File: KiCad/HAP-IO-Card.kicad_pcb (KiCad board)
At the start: 2 copper layers, 110 x 72 mm, 201 parts, among them CON601 AVR-JTAG-10, J201 DI1, J202 DI2, J203 DI3, J204 DI4, J205 DI5, J206 DI6, J207 DI7, J208 DI8, J209 DO1/2, J210 DO3/4, J211 DO5/6, J212 DO7/8, J213 GND, J214 GND, J215 GND, J216 GND, J401 AI1, J402 AI2, J403 AI3, J404 AI4, J405 AI5, J406 AI6, J407 AI7, J408 AI8, J501 12V, J601 ISP0, J602 ISP1, J603 CONN_01X02, J604 CONN_01X02, J605 CONN_01X02, J606 CONN_01X02, J607 CONN_01X03, J608 CONN_01X03, J701 NEO1, J702 5V_I/O_2, J703 5V_I/O_1, J704 NEO1, J705 NEO1, J706 NEO1, J707 NeoPixel, Q201 ZXTN25050DFHTA, Q202 ZXTN25050DFHTA, Q203 ZXTN25050DFHTA, Q204 ZXTN25050DFHTA, Q205 ZXTN25050DFHTA, Q206 ZXTN25050DFHTA, Q207 ZXTN25050DFHTA, Q208 ZXTN25050DFHTA, U201 LTV-354T, U202 LTV-354T, U203 LTV-354T, U204 LTV-354T, U205 LTV-354T, U206 LTV-354T, U207 LTV-354T, U208 LTV-354T, U209 MCP23017, U401 ADS1115IDGST, U402 ADS1115IDGST, U501 LM1086-5V, U502 LM1086-3.3V, U701 TXB0102DCT

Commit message: Remade layout
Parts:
- C201, C202, C203, C204, C205, C206, C207, C208, C409, C410, C701, C702, C704, R209, R210, R211, R212, R213, R214, R215, R216, R237, R238, R249, R250, R409, R410, R411, R412, U401, U402, U701: moved to F.Cu
- D215, D216, D217, D218, D219, D220, D223, D224: footprint Diodes_THT:D_DO-41_SOD81_P5.08mm_Vertical_KathodeUp -> Diodes_THT:D_DO-41_SOD81_P2.54mm_Vertical_KathodeUp
- J701: value NEO1 -> 5V_I/O_2; footprint Pin_Headers:Pin_Header_Straight_1x04_Pitch1.27mm -> Pin_Headers:Pin_Header_Straight_1x02_Pitch2.54mm
- J702: value 5V_I/O_2 -> 5V_I/O_1
- J703: value 5V_I/O_1 -> NEO1; footprint Pin_Headers:Pin_Header_Straight_1x02_Pitch2.54mm -> Pin_Headers:Pin_Header_Straight_1x04_Pitch1.27mm
- J704: value NEO1 -> NEO2
- J705: value NEO1 -> NEO3
- J706: value NEO1 -> NEO4
- J707: value NeoPixel -> CONN_01X03; footprint Pin_Headers:Pin_Header_Straight_1x01_Pitch2.54mm -> Pin_Headers:Pin_Header_Straight_1x03_Pitch2.54mm
- R225, R226, R227, R228, R229, R230: value 180 -> 10k; moved to F.Cu
- R231, R232: value 470 -> 10k; moved to F.Cu
- R233, R234, R235, R236: value 470 -> 180; moved to F.Cu
- R241, R242, R243, R244, R247, R248: value 10k -> 470
- R245, R246: value 10k -> 180; moved to F.Cu
- moved J603 142.0 mm to (-35.8, 19.5)
- moved J604 142.0 mm to (-26.3, 19.5)
- moved J605 142.0 mm to (-18.3, 19.5)
- moved J606 142.0 mm to (-10.3, 19.5)
- moved J607 142.0 mm to (-12.8, 24.0)
- moved J608 142.0 mm to (-12.8, 28.0)
- moved J707 102.7 mm to (193.7, -11.5)
- moved J701 101.1 mm to (179.2, -13.5)
- moved J703 101.1 mm to (179.7, -17.5)
- moved J704 101.1 mm to (186.7, -13.5)
- moved J705 101.1 mm to (179.2, -9.03)
- moved J706 101.1 mm to (186.7, -9.03)
- moved R225 83.5 mm to (50.2, 36.5), turned to 270 degrees
- moved J702 82.1 mm to (192.2, -20.5)
- moved R250 78.4 mm to (154.7, -16.0), turned to 270 degrees
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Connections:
- J701 pad 1: Net-(C704-Pad1) -> GND
- J701 pad 2: POWER5V -> Net-(C703-Pad1)
- J702 pad 1: Net-(C703-Pad1) -> GND
- J702 pad 2: GND -> Net-(C704-Pad1)
- J703 pad 2: GND -> POWER5V
- J704 pad 1: Net-(J701-Pad4) -> Net-(J703-Pad4)
- J707 pad 1: Net-(J706-Pad4) -> GND
- R225 pad 2: Net-(D209-Pad2) -> DI1
- R226 pad 2: Net-(D210-Pad2) -> DI2
- R227 pad 2: Net-(D211-Pad2) -> DI3
- R228 pad 2: Net-(D212-Pad2) -> DI4
- R229 pad 2: Net-(D213-Pad2) -> DI5
- R230 pad 2: Net-(D214-Pad2) -> DI6
- R231 pad 1: Net-(Q201-Pad1) -> POWER3V3
- R231 pad 2: DO1 -> DI7
- R232 pad 1: Net-(Q202-Pad1) -> POWER3V3
- R232 pad 2: DO2 -> DI8
- R233 pad 1: Net-(Q203-Pad1) -> POWER3V3
- R233 pad 2: DO3 -> Net-(D209-Pad2)
- R234 pad 1: Net-(Q204-Pad1) -> POWER3V3
- R234 pad 2: DO4 -> Net-(D210-Pad2)
- R235 pad 1: Net-(Q205-Pad1) -> POWER3V3
- R235 pad 2: DO5 -> Net-(D211-Pad2)
- R236 pad 1: Net-(Q206-Pad1) -> POWER3V3
- R236 pad 2: DO6 -> Net-(D212-Pad2)
- R237 pad 2: Net-(D221-Pad2) -> Net-(D213-Pad2)
- R238 pad 2: Net-(D222-Pad2) -> Net-(D214-Pad2)
- R239 pad 1: Net-(Q207-Pad1) -> Net-(Q201-Pad1)
- R239 pad 2: DO7 -> DO1
- R240 pad 1: Net-(Q208-Pad1) -> Net-(Q202-Pad1)
- R240 pad 2: DO8 -> DO2
- R241 pad 1: POWER3V3 -> Net-(Q203-Pad1)
- R241 pad 2: DIGITAL_INTB -> DO3
- R242 pad 1: POWER3V3 -> Net-(Q204-Pad1)
- R242 pad 2: DIGITAL_INTA -> DO4
- R243 pad 1: POWER3V3 -> Net-(Q205-Pad1)
- R243 pad 2: DI1 -> DO5
- R244 pad 1: POWER3V3 -> Net-(Q206-Pad1)
- R244 pad 2: DI2 -> DO6
- R245 pad 2: DI3 -> Net-(D221-Pad2)
- R246 pad 2: DI4 -> Net-(D222-Pad2)
- R247 pad 1: POWER3V3 -> Net-(Q207-Pad1)
- R247 pad 2: DI5 -> DO7
- R248 pad 1: POWER3V3 -> Net-(Q208-Pad1)
- R248 pad 2: DI6 -> DO8
- R249 pad 2: DI7 -> DIGITAL_INTB
- R250 pad 2: DI8 -> DIGITAL_INTA
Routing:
- net POWER3V3: track 77.8 -> 0.00 mm, vias 4 -> 0
- net ANALOG_RDY_1: track 57.1 -> 0.00 mm
- net DI8: track 54.5 -> 0.00 mm
- net DI7: track 50.0 -> 0.00 mm
- net DI6: track 44.6 -> 0.00 mm
- net ANALOG_SDA: track 41.4 -> 0.00 mm, vias 3 -> 0
- net DI5: track 40.1 -> 0.00 mm
- net ANALOG_SCL: track 38.2 -> 0.00 mm, vias 2 -> 0
- net DI4: track 28.9 -> 0.00 mm, vias 2 -> 0
- net ANALOG_RDY_2: track 27.1 -> 0.00 mm, vias 2 -> 0
- net DI1: track 24.1 -> 0.00 mm
- net DI3: track 23.4 -> 0.00 mm
- net AI4: track 22.5 -> 0.00 mm
- net AI5: track 22.4 -> 0.00 mm
- net AI1: track 22.1 -> 0.00 mm
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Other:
- board text added: "LogDbg"

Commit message: Before starting traces
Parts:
- C703: moved to F.Cu
- moved C703 140.6 mm to (51.2, 55.3), turned to 90 degrees
- moved C704 132.8 mm to (48.2, 55.3)
- moved C702 130.5 mm to (60.2, 55.3)
- moved U701 130.5 mm to (55.7, 55.3), turned to 0 degrees
- moved C701 129.3 mm to (59.2, 58.3), turned to 0 degrees
- moved C209 128.0 mm to (67.2, 55.5)
- moved R701 121.7 mm to (57.2, 51.3), turned to 0 degrees
- moved U209 111.0 mm to (78.0, 55.7), turned to 270 degrees
- moved J603 106.7 mm to (49.2, 83.9), turned to 0 degrees
- moved J604 102.7 mm to (53.7, 83.9), turned to 0 degrees
- moved J608 101.3 mm to (73.2, 81.4), turned to 0 degrees
- moved J605 100.0 mm to (58.2, 83.9), turned to 0 degrees
- moved J607 99.3 mm to (68.2, 81.4), turned to 0 degrees
- moved J606 97.8 mm to (63.2, 83.9), turned to 0 degrees
- moved R250 97.5 mm to (91.2, 58.0), turned to 0 degrees
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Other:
- board text added: "EspPwr"

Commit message: Save...
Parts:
- moved R232 2.90 mm to (124.6, 37.0)
- moved R223 2.57 mm to (110.2, 37.0), turned to 90 degrees
- moved R222 2.55 mm to (99.2, 37.0), turned to 90 degrees
- moved R230 2.55 mm to (101.7, 37.0)
- moved R231 2.52 mm to (112.7, 37.0)
- moved R224 2.20 mm to (122.1, 37.0), turned to 90 degrees
- moved C704 1.01 mm to (47.2, 55.5)
- moved R209 0.71 mm to (45.2, 33.0)
- moved R210 0.71 mm to (54.7, 33.0)
- moved R211 0.71 mm to (64.2, 33.0)
- moved C701 0.66 mm to (59.2, 59.0)
- moved C702 0.53 mm to (60.7, 55.5)
- moved C703 0.53 mm to (50.7, 55.5)
- moved C201 0.50 mm to (48.7, 40.0)
- moved C202 0.50 mm to (58.2, 40.0)
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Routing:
- net Net-(J202-Pad2): track 0.00 -> 6.23 mm
- net Net-(R201-Pad1): track 0.00 -> 5.61 mm, vias 0 -> 1
- net Net-(R202-Pad1): track 0.00 -> 5.41 mm, vias 0 -> 1
- net Net-(J202-Pad1): track 0.00 -> 5.34 mm
- net Net-(J201-Pad2): track 0.00 -> 5.00 mm
- net Net-(J201-Pad1): track 0.00 -> 4.41 mm
- net Net-(C202-Pad1): track 0.00 -> 3.41 mm
- net Net-(C201-Pad1): track 0.00 -> 3.41 mm
- net DI1: track 0.00 -> 2.80 mm
- net DI2: track 0.00 -> 2.80 mm
- net Net-(D201-Pad2): track 0.00 -> 1.03 mm
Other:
- board text added: "HAP I/O Card (C) Per Malmberg"

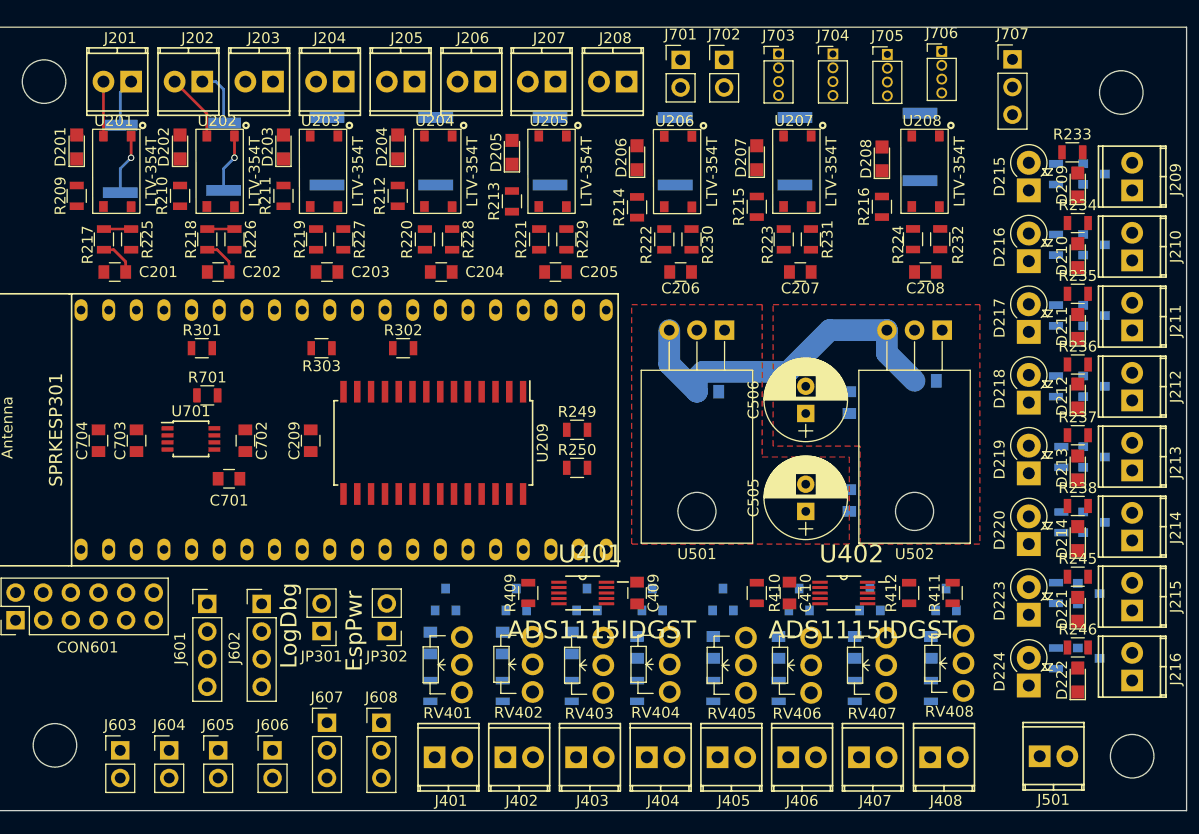
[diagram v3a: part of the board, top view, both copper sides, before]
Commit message: Before reworking analog inputs.
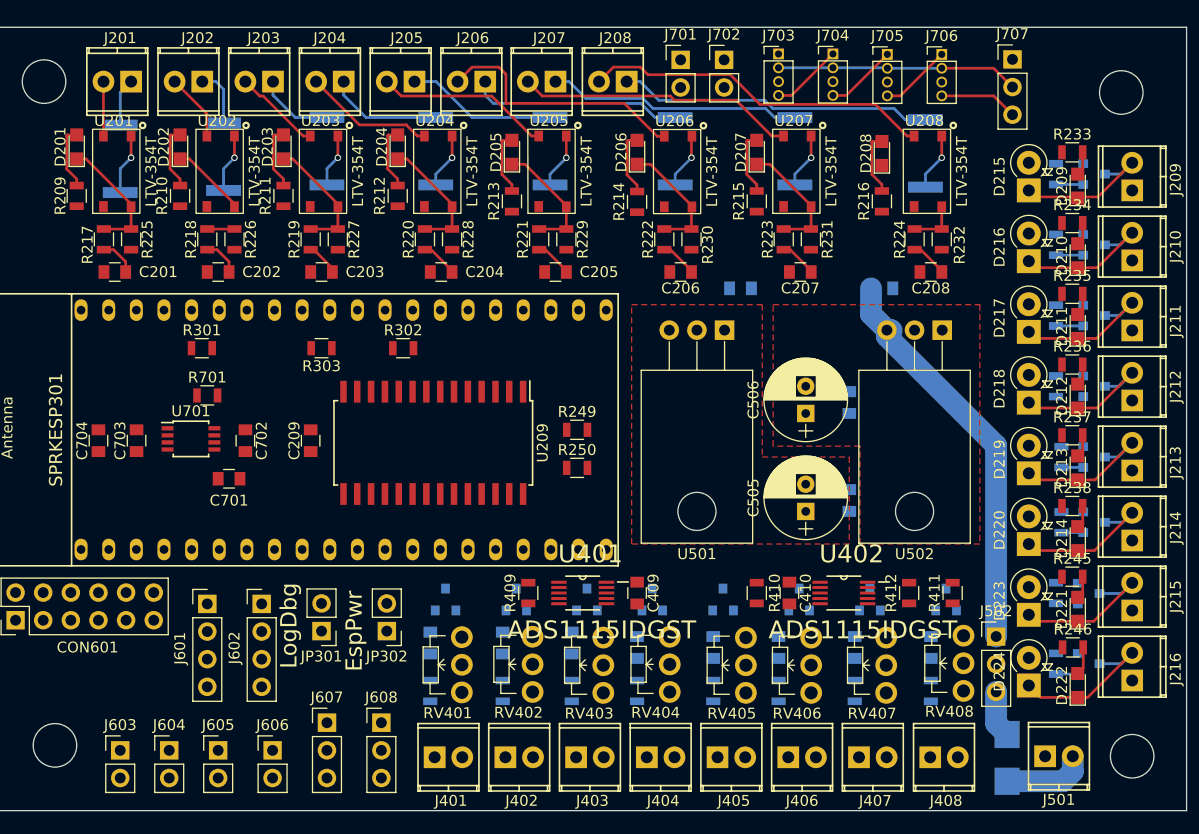
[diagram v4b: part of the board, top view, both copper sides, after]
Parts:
- added D501: MBR340, Diodes_SMD:D_SMB, B.Cu at (130.7, 84.6)
- added J502: CONN_01X03_FEMALE, Pin_Headers:Pin_Header_Straight_1x03_Pitch2.54mm, F.Cu at (129.7, 73.5)
- moved C501 9.96 mm to (106.2, 41.5)
- moved C502 9.39 mm to (119.2, 41.5)
- moved R208 0.78 mm to (123.2, 29.1)
- moved C203 0.50 mm to (67.7, 40.0)
- moved C208 0.50 mm to (123.7, 40.0)
- moved D206 0.50 mm to (96.7, 29.0)
- moved D207 0.50 mm to (107.7, 29.0)
- moved D208 0.50 mm to (119.2, 29.1)
- moved D222 0.50 mm to (137.2, 78.0)
- moved J501 0.50 mm to (134.2, 84.5)
- moved Q208 0.50 mm to (138.2, 76.0)
- moved R214 0.50 mm to (96.7, 33.5)
- moved R215 0.50 mm to (107.7, 33.5)
- moved R216 0.50 mm to (119.2, 33.5)
- moved R219 0.50 mm to (66.7, 37.0)
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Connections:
- J501 pad 2: /Powersupply/Input12V -> /Powersupply/Input12VOutside
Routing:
- net Net-(J208-Pad2): track 0.00 -> 32.1 mm
- net Net-(J208-Pad1): track 0.00 -> 28.9 mm
- net Net-(J207-Pad2): track 0.00 -> 25.6 mm
- net Net-(J206-Pad2): track 0.00 -> 23.7 mm
- net Net-(J207-Pad1): track 0.00 -> 23.4 mm
- net POWER5V: track 0.00 -> 22.2 mm
- net Net-(J206-Pad1): track 0.00 -> 19.6 mm
- net Net-(J205-Pad2): track 0.00 -> 16.0 mm
- net Net-(D222-Pad1): track 0.00 -> 15.1 mm
- net Net-(D221-Pad1): track 0.00 -> 14.6 mm
- net Net-(D213-Pad1): track 0.00 -> 14.2 mm
- net Net-(D211-Pad1): track 0.00 -> 14.1 mm
- net Net-(D212-Pad1): track 0.00 -> 14.1 mm
- net Net-(D214-Pad1): track 0.00 -> 14.0 mm
- net Net-(D210-Pad1): track 0.00 -> 14.0 mm
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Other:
- net class Input12VOutside added: clearance 0.2, trace_width 2, via_dia 0.6, via_drill 0.4
- net class Input12VOutside2 added: clearance 0.2, trace_width 2, via_dia 0.6, via_drill 0.4

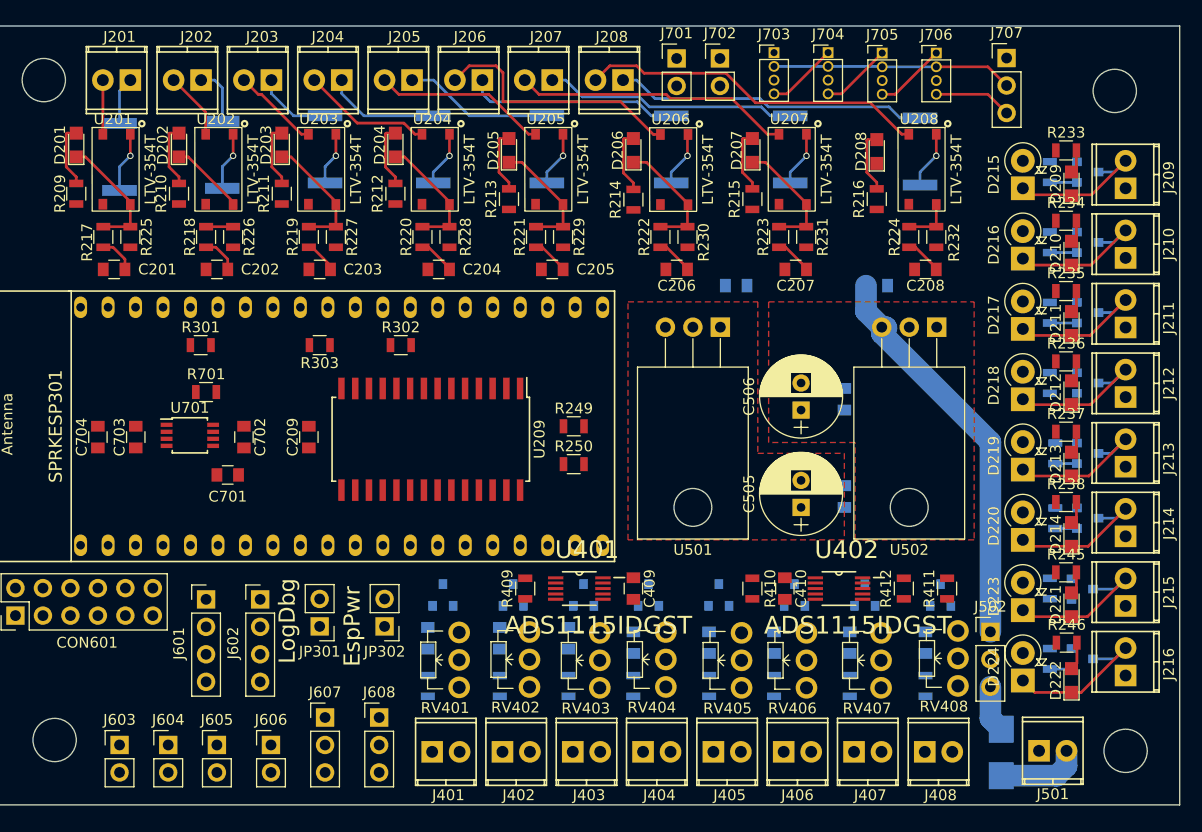
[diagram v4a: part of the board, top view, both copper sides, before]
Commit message: Inputs reworked. New terminals
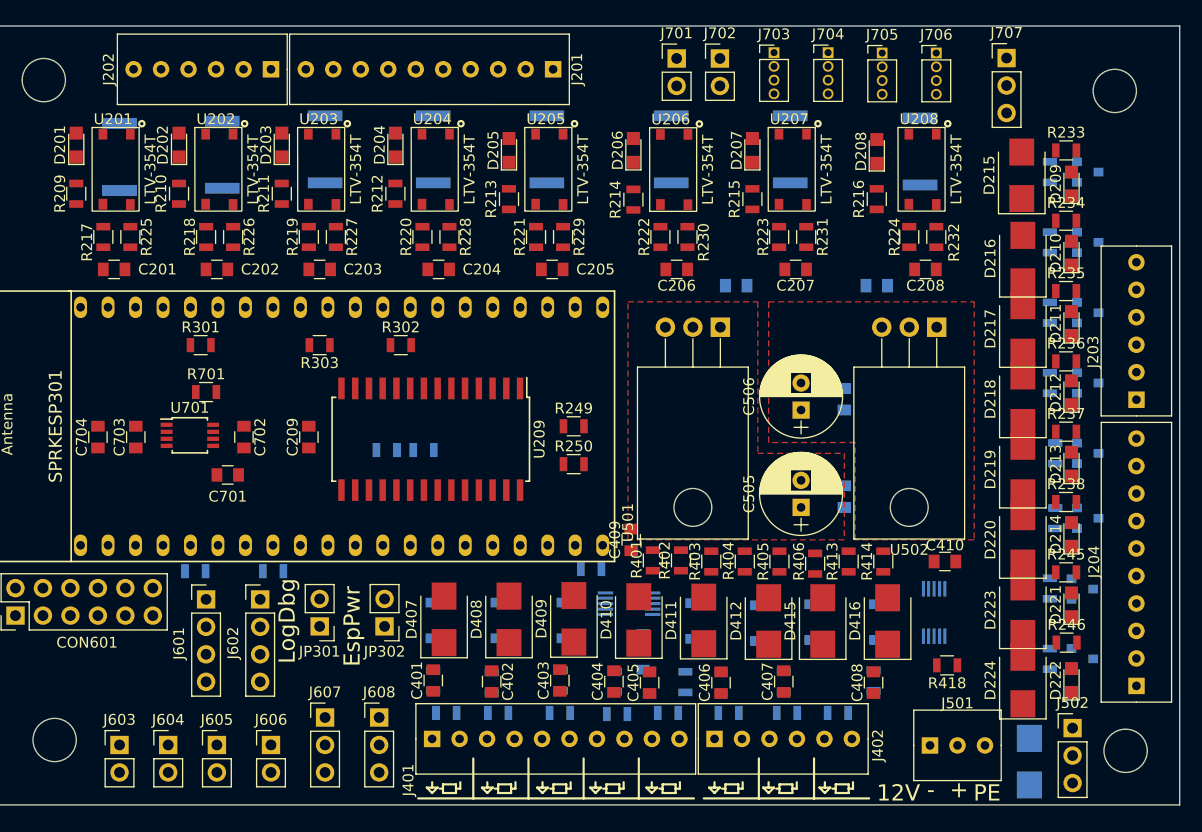
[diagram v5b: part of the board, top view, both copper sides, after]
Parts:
- removed J205: DI5, Connectors_Terminal_Blocks:TerminalBlock_Pheonix_MPT-2.54mm_2pol
- removed J206: DI6, Connectors_Terminal_Blocks:TerminalBlock_Pheonix_MPT-2.54mm_2pol
- removed J207: DI7, Connectors_Terminal_Blocks:TerminalBlock_Pheonix_MPT-2.54mm_2pol
- removed J208: DI8, Connectors_Terminal_Blocks:TerminalBlock_Pheonix_MPT-2.54mm_2pol
- removed J209: DO1/2, Connectors_Terminal_Blocks:TerminalBlock_Pheonix_MPT-2.54mm_2pol
- removed J210: DO3/4, Connectors_Terminal_Blocks:TerminalBlock_Pheonix_MPT-2.54mm_2pol
- removed J211: DO5/6, Connectors_Terminal_Blocks:TerminalBlock_Pheonix_MPT-2.54mm_2pol
- removed J212: DO7/8, Connectors_Terminal_Blocks:TerminalBlock_Pheonix_MPT-2.54mm_2pol
- removed J213, J214, J215, J216: GND, Connectors_Terminal_Blocks:TerminalBlock_Pheonix_MPT-2.54mm_2pol
- removed J403: AI3, Connectors_Terminal_Blocks:TerminalBlock_Pheonix_MPT-2.54mm_2pol
- removed J404: AI4, Connectors_Terminal_Blocks:TerminalBlock_Pheonix_MPT-2.54mm_2pol
- removed J405: AI5, Connectors_Terminal_Blocks:TerminalBlock_Pheonix_MPT-2.54mm_2pol
- removed J406: AI6, Connectors_Terminal_Blocks:TerminalBlock_Pheonix_MPT-2.54mm_2pol
- removed J407: AI7, Connectors_Terminal_Blocks:TerminalBlock_Pheonix_MPT-2.54mm_2pol
- removed J408: AI8, Connectors_Terminal_Blocks:TerminalBlock_Pheonix_MPT-2.54mm_2pol
- added D409: S1BB-13-F, Diodes_SMD:D_SMB, F.Cu at (91.2, 72.3)
- added D410: S1BB-13-F, Diodes_SMD:D_SMB, F.Cu at (97.2, 72.4)
- added D411: S1BB-13-F, Diodes_SMD:D_SMB, F.Cu at (103.2, 72.4)
- added D412: S1BB-13-F, Diodes_SMD:D_SMB, F.Cu at (109.2, 72.5)
- added D413: D_Schottky, Diodes_SMD:D_SOD-123, B.Cu at (113.1, 72.6)
- added D414: D_Schottky, Diodes_SMD:D_SOD-123, B.Cu at (119.1, 72.6)
- added D415: S1BB-13-F, Diodes_SMD:D_SMB, F.Cu at (114.2, 72.5)
- added D416: S1BB-13-F, Diodes_SMD:D_SMB, F.Cu at (120.2, 72.5)
- added R251: 10k, Resistors_SMD:R_0805, B.Cu at (77.3, 56.7)
- added R252: 10k, Resistors_SMD:R_0805, B.Cu at (73.9, 56.7)
- added R413: 2k, Resistors_SMD:R_0805, F.Cu at (116.6, 67.0)
- added R414: 2k, Resistors_SMD:R_0805, F.Cu at (119.8, 67.0)
- added R415: 499, Resistors_SMD:R_0805, B.Cu at (110.6, 78.1)
- added R416: 499, Resistors_SMD:R_0805, B.Cu at (118.9, 78.0)
- added R417: 10k, Resistors_SMD:R_0805, B.Cu at (92.8, 67.7)
- added R418: 10k, Resistors_SMD:R_0805, F.Cu at (125.7, 76.6)
- added R419: 10k, Resistors_SMD:R_0805, B.Cu at (63.4, 67.9)
- added R420: 10k, Resistors_SMD:R_0805, B.Cu at (56.2, 67.9)
- C401, C402, C403, C404, C405, C406, C407, C408: moved to F.Cu
- D215, D216, D217, D218, D219, D220, D223, D224: value 1N4007 -> S1BB-13-F; footprint Diodes_THT:D_DO-41_SOD81_P2.54mm_Vertical_KathodeUp -> Diodes_SMD:D_SMB
- D401, D402, D403, D404, D405, D406: value 3.3V -> D_Schottky; footprint Diodes_SMD:D_SOT-23_ANK -> Diodes_SMD:D_SOD-123
- D407, D408: value 3.3V -> S1BB-13-F; footprint Diodes_SMD:D_SOT-23_ANK -> Diodes_SMD:D_SMB; moved to F.Cu
- J201: value DI1 -> TE_Connectivity_1-282834-0; footprint Connectors_Terminal_Blocks:TerminalBlock_Pheonix_MPT-2.54mm_2pol -> TE_Connectivity:TE_Connectivity_1-282834-0
- J202: value DI2 -> TE_Connectivity_282834-6; footprint Connectors_Terminal_Blocks:TerminalBlock_Pheonix_MPT-2.54mm_2pol -> TE_Connectivity:TE_Connectivity_282834-6
- J203: value DI3 -> TE_Connectivity_282834-6; footprint Connectors_Terminal_Blocks:TerminalBlock_Pheonix_MPT-2.54mm_2pol -> TE_Connectivity:TE_Connectivity_282834-6
- J204: value DI4 -> TE_Connectivity_1-282834-0; footprint Connectors_Terminal_Blocks:TerminalBlock_Pheonix_MPT-2.54mm_2pol -> TE_Connectivity:TE_Connectivity_1-282834-0
- J401: value AI1 -> TE_Connectivity_1-282834-0; footprint Connectors_Terminal_Blocks:TerminalBlock_Pheonix_MPT-2.54mm_2pol -> TE_Connectivity:TE_Connectivity_1-282834-0
- J402: value AI2 -> TE_Connectivity_282834-6; footprint Connectors_Terminal_Blocks:TerminalBlock_Pheonix_MPT-2.54mm_2pol -> TE_Connectivity:TE_Connectivity_282834-6
- J501: value 12V -> TE_Connectivity_282834-3; footprint Connectors_Terminal_Blocks:TerminalBlock_Pheonix_MPT-2.54mm_2pol -> TE_Connectivity:TE_Connectivity_282834-3
- R401, R402, R403, R404, R405, R406: value 1K -> 2k; moved to F.Cu
- R407, R408: value 1K -> 499
- R409, R410, R411, R412: value 10k -> 499; moved to B.Cu
- RV401, RV402, RV403, RV404, RV405, RV406, RV407, RV408: value 10k -> Varistor; footprint Potentiometers:Potentiometer_WirePads_Small -> Resistors_SMD:R_0805; moved to B.Cu
- U401, U402: moved to B.Cu
- moved J204 92.4 mm to (143.2, 78.5), turned to 90 degrees
- moved J203 85.2 mm to (143.2, 52.0), turned to 90 degrees
- moved R408 40.1 mm to (83.6, 78.2)
- moved D408 40.0 mm to (85.2, 72.3)
- moved J201 39.1 mm to (89.3, 21.5)
- moved D407 39.0 mm to (79.2, 72.3)
- moved R407 38.5 mm to (78.2, 78.0)
- moved R411 25.7 mm to (101.5, 78.1), turned to 270 degrees
- moved R401 23.8 mm to (98.5, 66.9), turned to 90 degrees
- moved R402 20.4 mm to (101.1, 66.9)
- moved J402 19.6 mm to (104.2, 83.4)
- moved R412 19.0 mm to (104.8, 78.2)
- moved R403 17.5 mm to (103.9, 67.0)
- moved R404 15.4 mm to (107.0, 67.0)
- moved R410 15.3 mm to (95.0, 78.1)
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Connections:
- net /Powersupply/Input12VOutside2 renamed +12V
- net Net-(J201-Pad1) renamed /Digital I/O/DI1_1
- net Net-(J201-Pad2) renamed /Digital I/O/DI1_2
- C201 pad 2: GND -> Earth
- C202 pad 2: GND -> Earth
- C203 pad 2: GND -> Earth
- C204 pad 2: GND -> Earth
- C205 pad 2: GND -> Earth
- C206 pad 2: GND -> Earth
- C207 pad 2: GND -> Earth
- C208 pad 2: GND -> Earth
- C209 pad 2: GND -> Earth
- C401 pad 1: AI1 -> Net-(C401-Pad1)
- C401 pad 2: GND -> Earth
- C402 pad 1: AI2 -> Net-(C402-Pad1)
- C402 pad 2: GND -> Earth
- C403 pad 1: AI3 -> Net-(C403-Pad1)
- C403 pad 2: GND -> Earth
- C404 pad 1: AI4 -> Net-(C404-Pad1)
- C404 pad 2: GND -> Earth
- C405 pad 1: AI5 -> Net-(C405-Pad1)
- C405 pad 2: GND -> Earth
- C406 pad 1: AI6 -> Net-(C406-Pad1)
- C406 pad 2: GND -> Earth
- C407 pad 1: AI7 -> Net-(C407-Pad1)
- C407 pad 2: GND -> Earth
- C408 pad 1: AI8 -> Net-(C408-Pad1)
- C408 pad 2: GND -> Earth
- C409 pad 2: GND -> Earth
- C410 pad 2: GND -> Earth
- C501 pad 2: GND -> Earth
- C502 pad 2: GND -> Earth
- C503 pad 2: GND -> Earth
- C504 pad 2: GND -> Earth
- C505 pad 2: GND -> Earth
- C506 pad 2: GND -> Earth
- C701 pad 2: GND -> Earth
- C702 pad 2: GND -> Earth
- C703 pad 2: GND -> Earth
- C704 pad 2: GND -> Earth
- CON601 pad 10: GND -> Earth
- CON601 pad 2: GND -> Earth
- D209 pad 1: Net-(D209-Pad1) -> /Digital I/O/DO_1
- D210 pad 1: Net-(D210-Pad1) -> /Digital I/O/DO_2
- D211 pad 1: Net-(D211-Pad1) -> /Digital I/O/DO_3
- D212 pad 1: Net-(D212-Pad1) -> /Digital I/O/DO_4
- D213 pad 1: Net-(D213-Pad1) -> /Digital I/O/DO_5
- D214 pad 1: Net-(D214-Pad1) -> /Digital I/O/DO_6
- D215 pad 1: Net-(D209-Pad1) -> /Digital I/O/DO_1
- D215 pad 2: GND -> Earth
- D216 pad 1: Net-(D210-Pad1) -> /Digital I/O/DO_2
- D216 pad 2: GND -> Earth
- D217 pad 1: Net-(D211-Pad1) -> /Digital I/O/DO_3
- D217 pad 2: GND -> Earth
- D218 pad 1: Net-(D212-Pad1) -> /Digital I/O/DO_4
- D218 pad 2: GND -> Earth
- D219 pad 1: Net-(D213-Pad1) -> /Digital I/O/DO_5
- D219 pad 2: GND -> Earth
- D220 pad 1: Net-(D214-Pad1) -> /Digital I/O/DO_6
- D220 pad 2: GND -> Earth
- D221 pad 1: Net-(D221-Pad1) -> /Digital I/O/DO_7
- D222 pad 1: Net-(D222-Pad1) -> /Digital I/O/DO_8
- D223 pad 1: Net-(D221-Pad1) -> /Digital I/O/DO_7
- D223 pad 2: GND -> Earth
- D224 pad 1: Net-(D222-Pad1) -> /Digital I/O/DO_8
- D224 pad 2: GND -> Earth
- D401 pad 1: AI1 -> POWER5V
- D401 pad 2: GND -> Sense1
- D402 pad 1: AI2 -> POWER5V
- D402 pad 2: GND -> Sense2
- D403 pad 1: AI3 -> POWER5V
- D403 pad 2: GND -> Sense3
- D404 pad 1: AI4 -> POWER5V
- D404 pad 2: GND -> Sense4
- D405 pad 1: AI5 -> POWER5V
- D405 pad 2: GND -> Sense5
- D406 pad 1: AI6 -> POWER5V
- D406 pad 2: GND -> Sense6
- D407 pad 1: AI7 -> Net-(C401-Pad1)
- D407 pad 2: GND -> Sense1
- D408 pad 1: AI8 -> Net-(C402-Pad1)
- D408 pad 2: GND -> Sense2
- J202 pad 1: Net-(J202-Pad1) -> /Digital I/O/DI6_1
- J202 pad 2: Net-(J202-Pad2) -> /Digital I/O/DI6_2
- J203 pad 1: Net-(J203-Pad1) -> Earth
- J203 pad 2: Net-(J203-Pad2) -> /Digital I/O/DO_1
- J204 pad 1: Net-(J204-Pad1) -> Earth
- J204 pad 2: Net-(J204-Pad2) -> /Digital I/O/DO_4
- J401 pad 1: Net-(J401-Pad1) -> Earth
- J401 pad 2: GND -> /Sense Inputs/Sense1_DUT
- J402 pad 1: Net-(J402-Pad1) -> Earth
- J402 pad 2: GND -> /Sense Inputs/Sense6_DUT
- J501 pad 1: GND -> Earth
- J502 pad 2: GND -> Earth
- J603 pad 1: GND -> Earth
- J604 pad 1: GND -> Earth
- J605 pad 1: GND -> Earth
- J606 pad 1: GND -> Earth
- J607 pad 1: GND -> Earth
- J608 pad 1: GND -> Earth
- J701 pad 1: GND -> Earth
- J702 pad 1: GND -> Earth
- J703 pad 3: GND -> Earth
- J704 pad 3: GND -> Earth
- J705 pad 3: GND -> Earth
- J706 pad 3: GND -> Earth
- J707 pad 1: GND -> Earth
- JP301 pad 1: GND -> Earth
- Q201 pad 2: GND -> Earth
- Q201 pad 3: Net-(D209-Pad1) -> /Digital I/O/DO_1
- Q202 pad 2: GND -> Earth
- Q202 pad 3: Net-(D210-Pad1) -> /Digital I/O/DO_2
- Q203 pad 2: GND -> Earth
- Q203 pad 3: Net-(D211-Pad1) -> /Digital I/O/DO_3
- Q204 pad 2: GND -> Earth
- Q204 pad 3: Net-(D212-Pad1) -> /Digital I/O/DO_4
- Q205 pad 2: GND -> Earth
- Q205 pad 3: Net-(D213-Pad1) -> /Digital I/O/DO_5
- Q206 pad 2: GND -> Earth
- Q206 pad 3: Net-(D214-Pad1) -> /Digital I/O/DO_6
- Q207 pad 2: GND -> Earth
- Q207 pad 3: Net-(D221-Pad1) -> /Digital I/O/DO_7
- Q208 pad 2: GND -> Earth
- Q208 pad 3: Net-(D222-Pad1) -> /Digital I/O/DO_8
- R202 pad 2: Net-(J202-Pad1) -> /Digital I/O/DI2_1
- R203 pad 2: Net-(J203-Pad1) -> /Digital I/O/DI3_1
- R204 pad 2: Net-(J204-Pad1) -> /Digital I/O/DI4_1
- R205 pad 2: Net-(J205-Pad1) -> /Digital I/O/DI5_1
- R206 pad 2: Net-(J206-Pad1) -> /Digital I/O/DI6_1
- R207 pad 2: Net-(J207-Pad1) -> /Digital I/O/DI7_1
- R208 pad 2: Net-(J208-Pad1) -> /Digital I/O/DI8_1
- R249 pad 2: DIGITAL_INTB -> DIGITAL_I2C_SCL
- R250 pad 2: DIGITAL_INTA -> DIGITAL_I2C_SDA
- R401 pad 1: AI1 -> POWER5V
- R401 pad 2: Net-(R401-Pad2) -> Sense1
- R402 pad 1: AI2 -> POWER5V
- R402 pad 2: Net-(R402-Pad2) -> Sense2
- R403 pad 1: AI3 -> POWER5V
- R403 pad 2: Net-(R403-Pad2) -> Sense3
- R404 pad 1: AI4 -> POWER5V
- R404 pad 2: Net-(R404-Pad2) -> Sense4
- R405 pad 1: AI5 -> POWER5V
- R405 pad 2: Net-(R405-Pad2) -> Sense5
- R406 pad 1: AI6 -> POWER5V
- R406 pad 2: Net-(R406-Pad2) -> Sense6
- R407 pad 1: AI7 -> /Sense Inputs/Sense1_DUT
- R407 pad 2: Net-(R407-Pad2) -> Net-(C401-Pad1)
- R408 pad 1: AI8 -> /Sense Inputs/Sense2_DUT
- R408 pad 2: Net-(R408-Pad2) -> Net-(C402-Pad1)
- R409 pad 1: POWER3V3 -> /Sense Inputs/Sense3_DUT
- R409 pad 2: ANALOG_RDY_1 -> Net-(C403-Pad1)
- R410 pad 1: POWER3V3 -> /Sense Inputs/Sense4_DUT
- R410 pad 2: ANALOG_RDY_2 -> Net-(C404-Pad1)
- R411 pad 1: POWER3V3 -> /Sense Inputs/Sense5_DUT
- R411 pad 2: ANALOG_SDA -> Net-(C405-Pad1)
- R412 pad 1: POWER3V3 -> /Sense Inputs/Sense6_DUT
- R412 pad 2: ANALOG_SCL -> Net-(C406-Pad1)
- R701 pad 2: GND -> Earth
- RV401 pad 1: Net-(J401-Pad1) -> Earth
- RV401 pad 2: Net-(R401-Pad2) -> /Sense Inputs/Sense1_DUT
- RV402 pad 1: Net-(J402-Pad1) -> Earth
- RV402 pad 2: Net-(R402-Pad2) -> /Sense Inputs/Sense2_DUT
- RV403 pad 1: Net-(J403-Pad1) -> Earth
- RV403 pad 2: Net-(R403-Pad2) -> /Sense Inputs/Sense3_DUT
- RV404 pad 1: Net-(J404-Pad1) -> Earth
- RV404 pad 2: Net-(R404-Pad2) -> /Sense Inputs/Sense4_DUT
- RV405 pad 1: Net-(J405-Pad1) -> Earth
- RV405 pad 2: Net-(R405-Pad2) -> /Sense Inputs/Sense5_DUT
- RV406 pad 1: Net-(J406-Pad1) -> Earth
- RV406 pad 2: Net-(R406-Pad2) -> /Sense Inputs/Sense6_DUT
- RV407 pad 1: Net-(J407-Pad1) -> Earth
- RV407 pad 2: Net-(R407-Pad2) -> /Sense Inputs/Sense7_DUT
- RV408 pad 1: Net-(J408-Pad1) -> Earth
- RV408 pad 2: Net-(R408-Pad2) -> /Sense Inputs/Sense8_DUT
- SPRKESP301 pad 1: ANALOG_RDY_1 -> SENSE_RDY_1
- SPRKESP301 pad 17: GND -> Earth
- SPRKESP301 pad 2: ANALOG_RDY_2 -> SENSE_RDY_2
- SPRKESP301 pad 20: GND -> Earth
- SPRKESP301 pad 21: GND -> Earth
- SPRKESP301 pad 24: GND -> Earth
- SPRKESP301 pad 40: GND -> Earth
- SPRKESP301 pad 5: ANALOG_SCL -> SENSE_SCL
- SPRKESP301 pad 6: ANALOG_SDA -> SENSE_SDA
- U201 pad 4: GND -> Earth
- U202 pad 3: Net-(J202-Pad2) -> /Digital I/O/DI2_2
- U202 pad 4: GND -> Earth
- U203 pad 3: Net-(J203-Pad2) -> /Digital I/O/DI3_2
- U203 pad 4: GND -> Earth
- U204 pad 3: Net-(J204-Pad2) -> /Digital I/O/DI4_2
- U204 pad 4: GND -> Earth
- U205 pad 3: Net-(J205-Pad2) -> /Digital I/O/DI5_2
- U205 pad 4: GND -> Earth
- U206 pad 3: Net-(J206-Pad2) -> /Digital I/O/DI6_2
- U206 pad 4: GND -> Earth
- U207 pad 3: Net-(J207-Pad2) -> /Digital I/O/DI7_2
- U207 pad 4: GND -> Earth
- U208 pad 3: Net-(J208-Pad2) -> /Digital I/O/DI8_2
- U208 pad 4: GND -> Earth
- U209 pad 10: GND -> Earth
- U209 pad 15: GND -> Earth
- U401 pad 1: GND -> Earth
- U401 pad 10: ANALOG_SCL -> SENSE_SCL
- U401 pad 2: ANALOG_RDY_1 -> SENSE_RDY_1
- U401 pad 3: GND -> Earth
- U401 pad 4: AI1 -> Sense1
- U401 pad 5: AI2 -> Sense2
- U401 pad 6: AI3 -> Sense3
- U401 pad 7: AI4 -> Sense4
- U401 pad 9: ANALOG_SDA -> SENSE_SDA
- U402 pad 10: ANALOG_SCL -> SENSE_SCL
- U402 pad 2: ANALOG_RDY_2 -> SENSE_RDY_2
- U402 pad 3: GND -> Earth
- U402 pad 4: AI5 -> Sense5
- U402 pad 5: AI6 -> Sense6
- U402 pad 6: AI7 -> Sense7
- U402 pad 7: AI8 -> Sense8
- U402 pad 9: ANALOG_SDA -> SENSE_SDA
- U501 pad 1: GND -> Earth
- U502 pad 1: GND -> Earth
- U701 pad 2: GND -> Earth
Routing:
- net /Powersupply/Input12V: track 37.2 -> 0.00 mm
- net Net-(J208-Pad2): track 32.1 -> 0.00 mm
- net Net-(J208-Pad1): track 28.9 -> 0.00 mm
- net Net-(J207-Pad2): track 25.6 -> 0.00 mm
- net Net-(J206-Pad2): track 23.7 -> 0.00 mm
- net Net-(J207-Pad1): track 23.4 -> 0.00 mm
- net POWER5V: track 22.2 -> 0.00 mm
- net Net-(J206-Pad1): track 19.6 -> 0.00 mm
- net Net-(J205-Pad2): track 16.0 -> 0.00 mm
- net Net-(D222-Pad1): track 15.1 -> 0.00 mm
- net Net-(D221-Pad1): track 14.6 -> 0.00 mm
- net Net-(D213-Pad1): track 14.2 -> 0.00 mm
- net Net-(D211-Pad1): track 14.1 -> 0.00 mm
- net Net-(D212-Pad1): track 14.1 -> 0.00 mm
- net Net-(D214-Pad1): track 14.0 -> 0.00 mm
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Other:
- board text added: "+"
- board text added: "-"
- board text added: "12V"
- board text added: "PE"
